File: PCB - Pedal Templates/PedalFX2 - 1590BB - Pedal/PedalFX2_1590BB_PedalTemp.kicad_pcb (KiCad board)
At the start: 2 copper layers, 114.5 x 40.1 mm, 12 parts, among them J1 Conn_01x04_Female, T1 ACJS-MHDR, T2 ACJS-MHDR, T3 54-00129

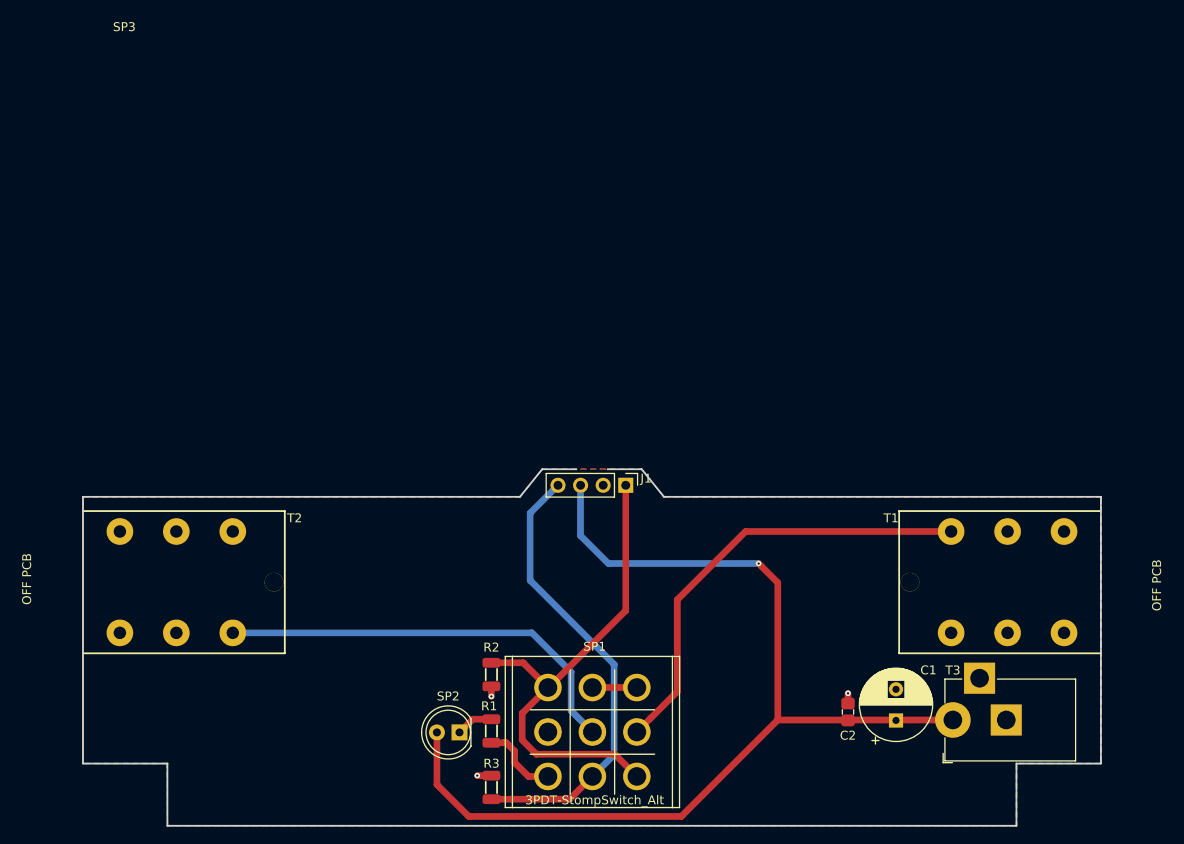
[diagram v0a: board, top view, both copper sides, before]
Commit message: Templates
Added pedal templates for each size of PedalFX2
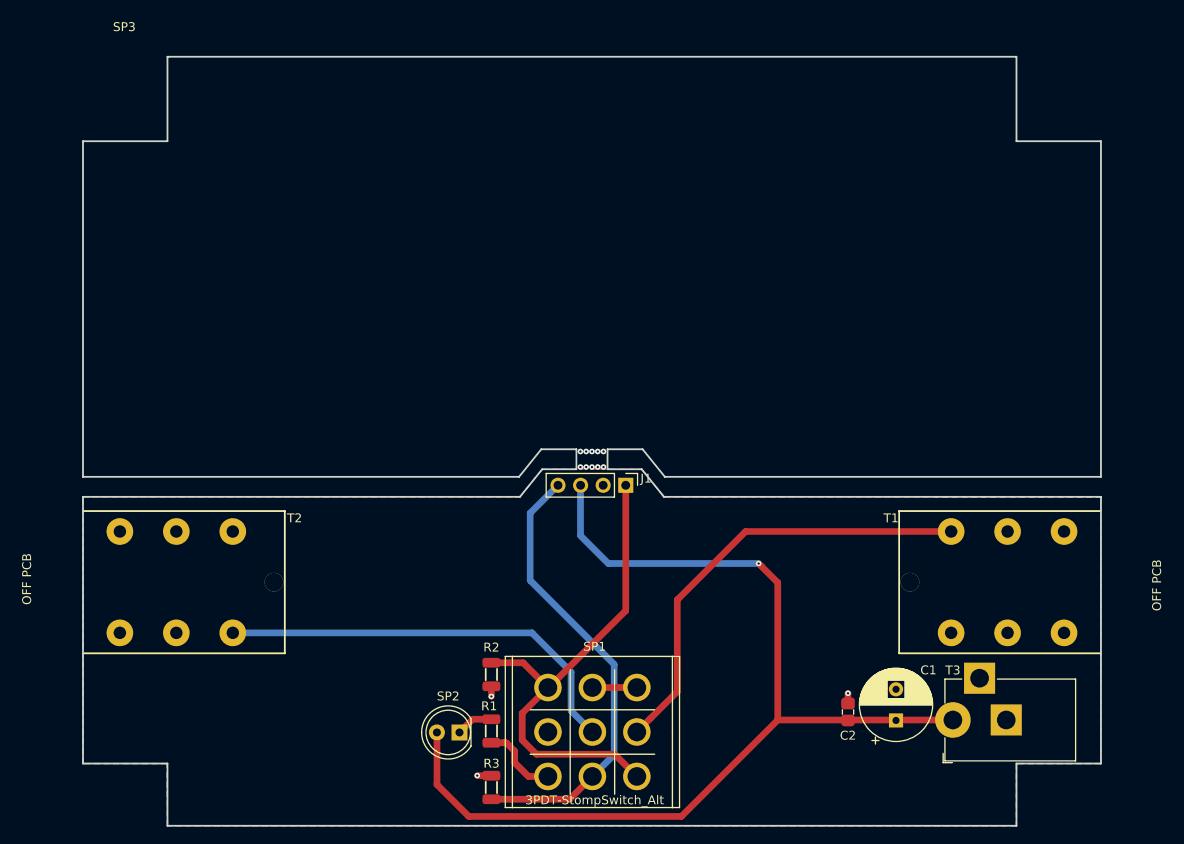
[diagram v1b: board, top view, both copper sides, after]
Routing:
- net (no net): vias 0 -> 10
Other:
- board size 114.5 x 40.1 mm -> 114.5 x 86.5 mm
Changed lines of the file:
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@@
   (general
     (thickness 1.6)
-    (drawings 25)
-    (tracks 56)
+    (drawings 40)
+    (tracks 66)
     (zones 0)
     (modules 12)
@@
   (gr_line (start 149.15 109.9) (end 153 109.9) (layer Edge.Cuts) (width 0.2))
   (gr_line (start 160.35 109.9) (end 156.5 109.9) (layer Edge.Cuts) (width 0.2))
+  (gr_line (start 160.45 107.65) (end 156.5 107.65) (layer Edge.Cuts) (width 0.2))
+  (gr_line (start 153 107.65) (end 149.05 107.65) (layer Edge.Cuts) (width 0.2))
+  (gr_line (start 153 109.9) (end 153 107.65) (layer Edge.Cuts) (width 0.2))
+  (gr_line (start 156.5 109.9) (end 156.5 107.65) (layer Edge.Cuts) (width 0.2))
+  (gr_line (start 212 110.75) (end 212 73) (layer Edge.Cuts) (width 0.2))
+  (gr_line (start 202.5 73) (end 212 73) (layer Edge.Cuts) (width 0.2))
+  (gr_line (start 202.5 63.5) (end 202.5 73) (layer Edge.Cuts) (width 0.2))
+  (gr_line (start 202.5 63.5) (end 107 63.5) (layer Edge.Cuts) (width 0.2))
+  (gr_line (start 107 63.5) (end 107 73) (layer Edge.Cuts) (width 0.2))
+  (gr_line (start 107 73) (end 97.5 73) (layer Edge.Cuts) (width 0.2))
+  (gr_line (start 97.5 110.75) (end 97.5 73) (layer Edge.Cuts) (width 0.2))
+  (gr_line (start 97.5 110.75) (end 146.55 110.75) (layer Edge.Cuts) (width 0.2))
+  (gr_line (start 146.55 110.75) (end 149.05 107.65) (layer Edge.Cuts) (width 0.2))
+  (gr_line (start 160.45 107.65) (end 162.95 110.75) (layer Edge.Cuts) (width 0.2))
+  (gr_line (start 212 110.75) (end 162.95 110.75) (layer Edge.Cuts) (width 0.2))
   (gr_line (start 202.3 142.8) (end 202.3 149.8) (layer Margin) (width 0.15))
   (gr_line (start 211.8 142.8) (end 202.3 142.8) (layer Margin) (width 0.15))
@@
   (gr_line (start 107 150) (end 107 143) (layer Edge.Cuts) (width 0.2))
   (gr_line (start 202.5 150) (end 107 150) (layer Edge.Cuts) (width 0.2))
+  (via (at 153.45 107.9) (size 0.635) (drill 0.254) (layers F.Cu B.Cu) (net 0))
+  (via (at 154.1 107.9) (size 0.635) (drill 0.254) (layers F.Cu B.Cu) (net 0))
+  (via (at 154.75 107.9) (size 0.635) (drill 0.254) (layers F.Cu B.Cu) (net 0))
+  (via (at 155.4 107.9) (size 0.635) (drill 0.254) (layers F.Cu B.Cu) (net 0))
+  (via (at 156.05 107.9) (size 0.635) (drill 0.254) (layers F.Cu B.Cu) (net 0))
+  (via (at 154.75 109.65) (size 0.635) (drill 0.254) (layers F.Cu B.Cu) (net 0))
+  (via (at 154.1 109.65) (size 0.635) (drill 0.254) (layers F.Cu B.Cu) (net 0))
+  (via (at 155.4 109.65) (size 0.635) (drill 0.254) (layers F.Cu B.Cu) (net 0))
+  (via (at 156.05 109.65) (size 0.635) (drill 0.254) (layers F.Cu B.Cu) (net 0))
+  (via (at 153.45 109.65) (size 0.635) (drill 0.254) (layers F.Cu B.Cu) (net 0))
   (via (at 141.85 144.35) (size 0.635) (drill 0.254) (layers F.Cu B.Cu) (net 1))
   (via (at 143.438 135.45) (size 0.635) (drill 0.254) (layers F.Cu B.Cu) (net 1))
